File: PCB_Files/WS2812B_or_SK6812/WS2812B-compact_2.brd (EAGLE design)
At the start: 40 x 25 mm, 41 parts, among them P1 HT7333

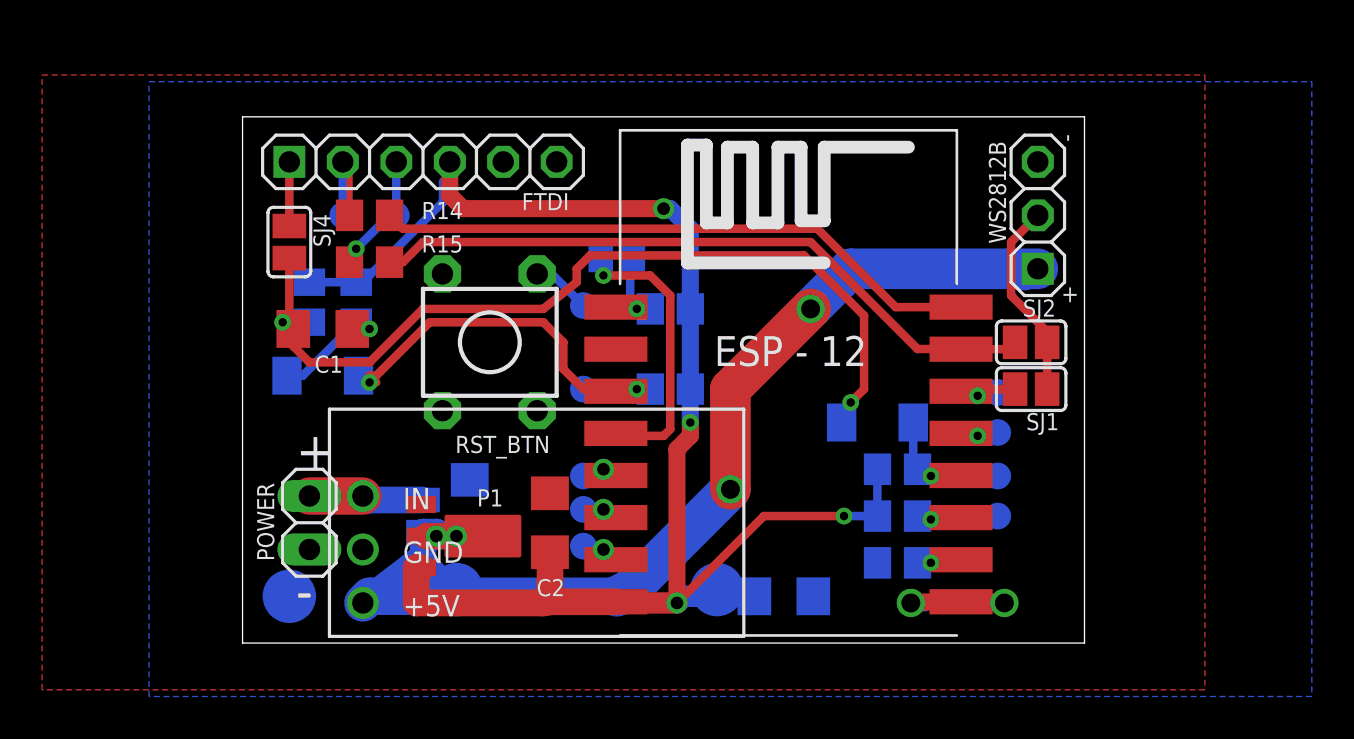
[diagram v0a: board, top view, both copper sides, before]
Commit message: created additional compact design of ws2812b module
this new design features smaller footprint, but the esp module ist partially outside the board, which will result in better wifi connection.

additionally the footprint of the HT7333 has been fixed as previously it had used the wrong package.
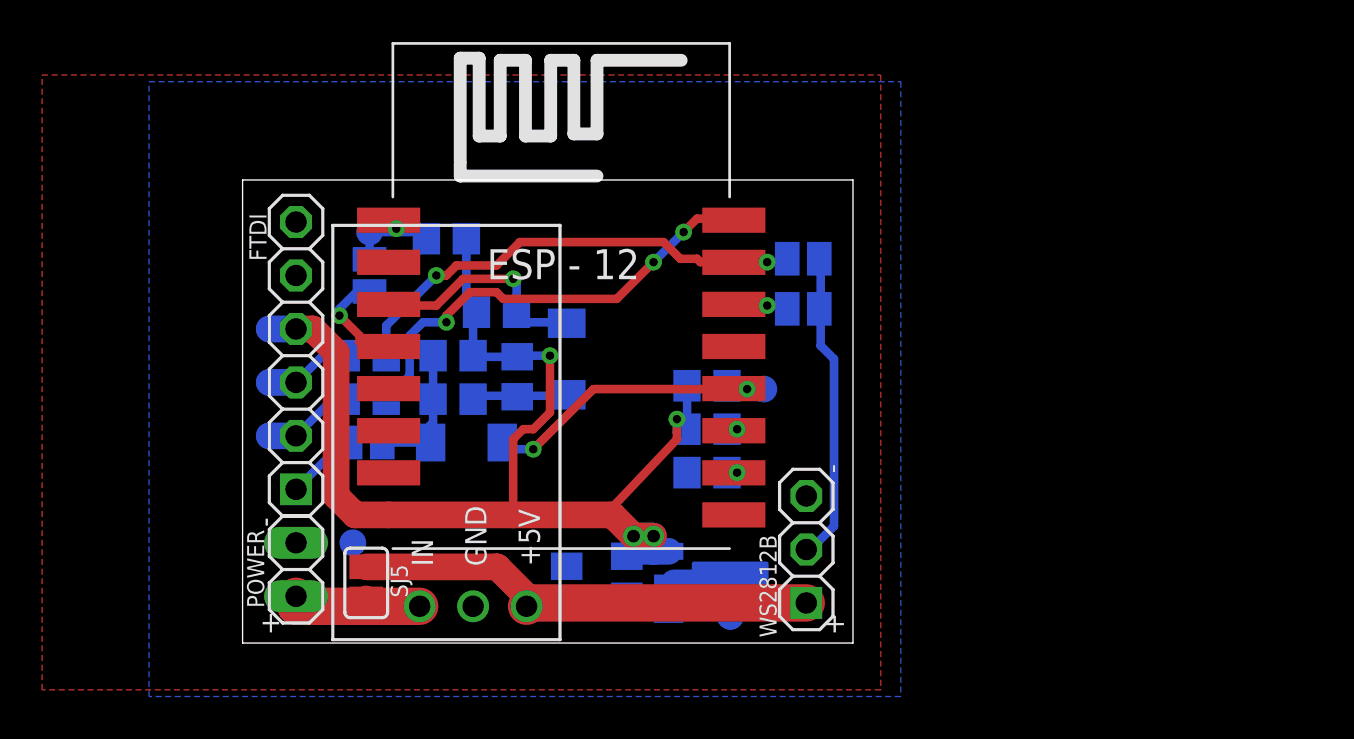
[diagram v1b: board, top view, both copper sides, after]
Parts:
- removed C5: 10u, rcl:C1206
- removed CH_PD, GP12, GP13, GP14, GP2, GP4, GP5: TPB1,27, testpad:B1,27
- removed RST_BTN: (no value), schalter_taster:KSM611A
- 3V3, 5V, GND: value TPB2,54 -> TPB1,27; device testpad:B2,54 -> testpad:B1,27
- C1: value 100n -> 10n; device rcl:C1206 -> rcl:C0805
- C2, C3: device rcl:C1206 -> rcl:C0805
- P1: value HT7333 -> HT7333SOT89
- R1, R2: value 100k -> 10k
- R11, R12: value 10k -> 4k7
- moved 3V3 24.6 mm to (1.27, 14.9), turned to 180 degrees
- moved D2 19.5 mm to (10.6, 9.53)
- moved WS2812B 19.3 mm to (26.8, 4.45)
- moved 5V 13.1 mm to (23.2, 1.27), turned to 0 degrees
- moved P1 12.0 mm to (22.2, 2.86), flipped to the bottom, turned to 90 degrees
- moved GP0 11.9 mm to (24.8, 12.1)
- moved SJ3 11.8 mm to (6.03, 17.5), turned to 270 degrees
- moved D3 11.6 mm to (15.4, 13.5), turned to 90 degrees
- moved U2 11.6 mm to (15.2, 14.3)
- moved SJ2 11.5 mm to (26.6, 18.3), flipped to the bottom, turned to 0 degrees
- moved SJ1 11.5 mm to (26.6, 15.9), flipped to the bottom, turned to 0 degrees
- moved R8 11.1 mm to (9.68, 19.2)
- moved TX 11.0 mm to (1.27, 9.84)
- moved FTDI 11.0 mm to (2.54, 13.7), turned to 90 degrees
- moved RST 10.7 mm to (6.03, 19.5), turned to 180 degrees
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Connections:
- removed net GP12: GP12.TP, U2.GPIO12
- removed net GP13: GP13.TP, U2.GPIO13
- removed net GP14: GP14.TP, U2.GPIO14
- removed net GP5: GP5.TP, U2.GPIO5
- net +3V3: no longer C5.1
- net CH_PD: no longer CH_PD.TP
- net GND: no longer C5.2, RST_BTN.B, RST_BTN.D
- net GP4: no longer GP4.TP
- net N$5: no longer GP2.TP
- net RST: no longer RST_BTN.A
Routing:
- net N$2: track 42.9 -> 6.82 mm, vias 2 -> 0
- net +5V: track 54.4 -> 32.2 mm, vias 4 -> 0
- net +3V3: track 76.9 -> 58.8 mm
- net ERX: track 32.5 -> 22.7 mm, vias 0 -> 2
- net CH_PD: track 20.5 -> 11.0 mm, vias 2 -> 1
- net N$6: track 13.8 -> 5.61 mm
- net GP0: track 7.68 -> 15.0 mm, vias 1 -> 2
- net GND: track 7.22 -> 0.00 mm, vias 2 -> 0
- net N$7: track 29.0 -> 22.0 mm, vias 0 -> 3
- net N$5: track 6.34 -> 0.65 mm
- net WS2812B-DATA: track 9.76 -> 14.9 mm
- net RST: track 11.2 -> 6.29 mm
- net GP12: track 2.02 -> 0.00 mm, vias 1 -> 0
- net GP13: track 2.00 -> 0.00 mm, vias 1 -> 0
- net GP5: track 1.86 -> 0.00 mm, vias 1 -> 0
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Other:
- board size 40 x 25 mm -> 29 x 22 mm
